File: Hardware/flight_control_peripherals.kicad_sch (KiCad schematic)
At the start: 17 parts, among them J10 Conn_02x06_Odd_Even, J11 Conn_01x06, J12 Micro_SD_Card_Det1, J6 Conn_01x10, J7 Conn_02x10_Odd_Even, J8 Conn_01x04, J9 Conn_01x04, U13 W25N01GVZEIG_TR, U14 24CW1280T-I/OT, U15 PCA9685PW_118

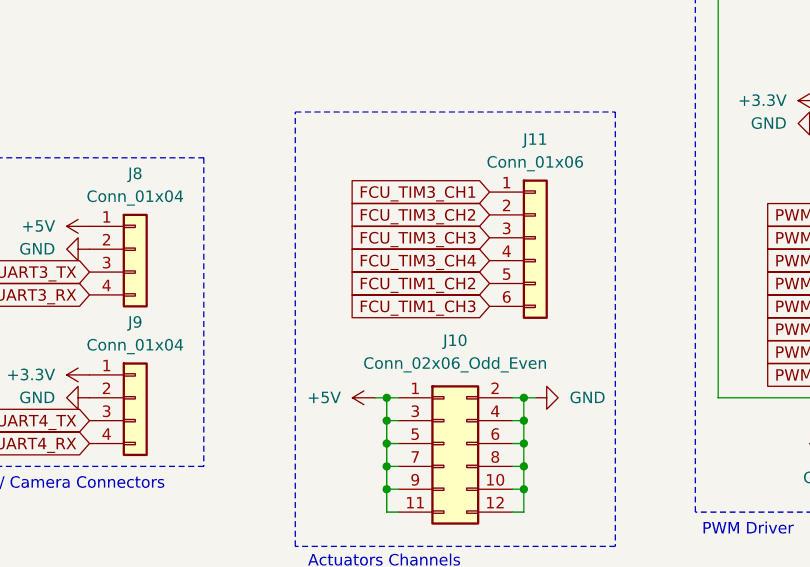
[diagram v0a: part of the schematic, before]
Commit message: fixed some errors in global labels
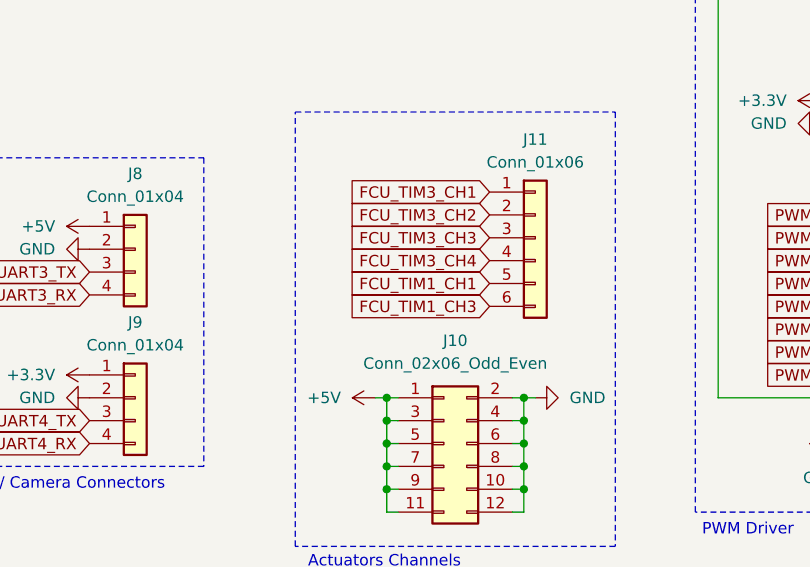
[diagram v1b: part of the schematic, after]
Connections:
- net FCU_TIM1_CH2 renamed FCU_TIM1_CH1
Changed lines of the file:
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@@
 		)
 	)
-	(global_label "FCU_TIM1_CH2"
+	(global_label "FCU_TIM1_CH1"
 		(shape input)
 		(at 172.72 62.23 180)
